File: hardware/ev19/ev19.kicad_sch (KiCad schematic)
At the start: 163 parts, among them CN1 Conn_05x02_Female, J1 USB_C_Receptacle, J10 USB_C_Receptacle, J11 Conn_02x05_Counter_Clockwise, J2 Conn_01x02_Socket, J4 Conn_02x03_Odd_Even, J5 Conn_02x03_Odd_Even, J6 Conn_02x05_Counter_Clockwise, J7 Conn_02x05_Counter_Clockwise, J8 Conn_02x05_Counter_Clockwise, J9 Conn_02x05_Counter_Clockwise, Q1 2N7002, Q2 2N7002, Q3 2N7002, Q4 2N7002, SW1 SW_SPDT, SW2 SW_Push, SW3 SW_Push, U1 BQ21040DBV, U12 XC6227C301MR-G, U2 USBLC6-2P6, U3 STM32F072CBTx, U4 CH340C, U5 TPS63060, U7 ESP32-S3-WROOM-1, U9 TPS2116DRL, Y1 Crystal_GND24

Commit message: Added missing footprints, used kicad10 wizard tool to design them, designed starting point of the board layout
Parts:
- removed J10: USB_C_Receptacle, Connector_USB:USB_C_Receptacle_HRO_TYPE-C-31-M-12, symbol Connector:USB_C_Receptacle_USB2.0_16P
- added H5: MountingHole, MountingHole:MountingHole_2.7mm_M2.5, symbol Mechanical:MountingHole
- added J13: USB_C_Receptacle_USB2.0_16P, Connector_USB:USB_C_Receptacle_HRO_TYPE-C-31-M-12, symbol Connector:USB_C_Receptacle_USB2.0_16P
- JP1: footprint (none) -> Jumper:SolderJumper-3_P1.3mm_Bridged12_RoundedPad1.0x1.5mm
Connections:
- new net: J13.A1 (GND), J13.A12 (GND), J13.B1 (GND), J13.B12 (GND)
- new net: J13.A4 (VBUS), J13.A9 (VBUS), J13.B4 (VBUS), J13.B9 (VBUS)
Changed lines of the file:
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@@
 	(rectangle
 		(start 153.67 222.25)
-		(end 180.34 247.65)
+		(end 180.34 251.46)
 		(stroke
 			(width 0)
@@
 	)
 	(symbol
+		(lib_id "Mechanical:MountingHole")
+		(at 158.75 247.65 0)
+		(unit 1)
+		(body_style 1)
+		(exclude_from_sim no)
+		(in_bom no)
+		(on_board yes)
+		(in_pos_files yes)
+		(dnp no)
+		(fields_autoplaced yes)
+		(property "Reference" "H5"
+			(at 161.29 246.3799 0)
+			(show_name no)
+			(do_not_autoplace no)
+			(effects
+				(font
+					(size 1.27 1.27)
+				)
+				(justify left)
+			)
+		)
+		(property "Value" "MountingHole"
+			(at 161.29 248.9199 0)
+			(show_name no)
+			(do_not_autoplace no)
+			(effects
+				(font
+					(size 1.27 1.27)
+				)
+				(justify left)
+			)
+		)
+		(property "Footprint" "MountingHole:MountingHole_2.7mm_M2.5"
+			(at 158.75 247.65 0)
+			(hide yes)
+			(show_name no)
+			(do_not_autoplace no)
+			(effects
+				(font
+					(size 1.27 1.27)
+				)
+			)
+		)
+		(property "Datasheet" ""
+			(at 158.75 247.65 0)
+			(hide yes)
+			(show_name no)
+			(do_not_autoplace no)
+			(effects
+				(font
+					(size 1.27 1.27)
+				)
+			)
+		)
+		(property "Description" "Mounting Hole without connection"
+			(at 158.75 247.65 0)
+			(hide yes)
+			(show_name no)
+			(do_not_autoplace no)
+			(effects
+				(font
+					(size 1.27 1.27)
+				)
+			)
+		)
+		(property "JLCPCB Position Offset" ""
+			(at 158.75 247.65 0)
+			(hide yes)
+			(show_name no)
+			(do_not_autoplace no)
+			(effects
+				(font
+					(size 1.27 1.27)
+				)
+			)
+		)
+		(property "Sim.Type" ""
+			(at 158.75 247.65 0)
+			(hide yes)
+			(show_name no)
+			(do_not_autoplace no)
+			(effects
+				(font
+					(size 1.27 1.27)
+				)
+			)
+		)
+		(instances
+			(project "ev19"
+				(path "/bd865368-262b-4f76-b7a6-1673c2cb0f8c"
+					(reference "H5")
+					(unit 1)
+				)
+			)
+		)
+	)
+	(symbol
 		(lib_id "Transistor_FET:2N7002")
 		(at 339.09 80.01 0)
@@
 	)
 	(symbol
-		(lib_id "Connector:USB_C_Receptacle_USB2.0_16P")
-		(at 539.75 345.44 0)
-		(unit 1)
-		(body_style 1)
-		(exclude_from_sim no)
-		(in_bom yes)
-		(on_board yes)
-		(in_pos_files yes)
-		(dnp no)
-		(property "Reference" "J10"
-			(at 550.164 326.644 0)
-			(show_name no)
-			(do_not_autoplace no)
-			(effects
-				(font
-					(size 1.27 1.27)
-				)
-				(justify right)
-			)
-		)
-		(property "Value" "USB_C_Receptacle"
-			(at 557.276 364.49 0)
-			(show_name no)
-			(do_not_autoplace no)
-			(effects
-				(font
-					(size 1.27 1.27)
-				)
-				(justify right)
-			)
-		)
-		(property "Footprint" "Connector_USB:USB_C_Receptacle_HRO_TYPE-C-31-M-12"
-			(at 543.56 345.44 0)
-			(hide yes)
-			(show_name no)
-			(do_not_autoplace no)
-			(effects
-				(font
-					(size 1.27 1.27)
-				)
-			)
-		)
-		(property "Datasheet" "https://www.usb.org/sites/default/files/documents/usb_type-c.zip"
-			(at 543.56 345.44 0)
-			(hide yes)
-			(show_name no)
-			(do_not_autoplace no)
-			(effects
-				(font
-					(size 1.27 1.27)
-				)
-			)
-		)
-		(property "Description" "USB 2.0-only 16P Type-C Receptacle connector"
-			(at 539.75 345.44 0)
-			(hide yes)
-			(show_name no)
-			(do_not_autoplace no)
-			(effects
-				(font
-					(size 1.27 1.27)
-				)
-			)
-		)
-		(property "JLCPCB Part #" "C165948"
-			(at 539.75 345.44 0)
-			(hide yes)
-			(show_name no)
-			(do_not_autoplace no)
-			(effects
-				(font
-					(size 1.27 1.27)
-				)
-			)
-		)
-		(property "JLCPCB Position Offset" ""
-			(at 539.75 345.44 0)
-			(hide yes)
-			(show_name no)
-			(do_not_autoplace no)
-			(effects
-				(font
-					(size 1.27 1.27)
-				)
-			)
-		)
-		(property "Sim.Type" ""
-			(at 539.75 345.44 0)
-			(hide yes)
-			(show_name no)
-			(do_not_autoplace no)
-			(effects
-				(font
-					(size 1.27 1.27)
-				)
-			)
-		)
-		(pin "A1"
-		)
-		(pin "A12"
-		)
-		(pin "A4"
-		)
-		(pin "A5"
-		)
-		(pin "A6"
-		)
-		(pin "A7"
-		)
-		(pin "A8"
-		)
-		(pin "A9"
-		)
-		(pin "B1"
-		)
-		(pin "B12"
-		)
-		(pin "B4"
-		)
-		(pin "B5"
-		)
-		(pin "B6"
-		)
-		(pin "B7"
-		)
-		(pin "B8"
-		)
-		(pin "B9"
-		)
-		(pin "S1"
-		)
-		(instances
-			(project "ev19"
-				(path "/bd865368-262b-4f76-b7a6-1673c2cb0f8c"
-					(reference "J10")
-					(unit 1)
-				)
-			)
-		)
-	)
-	(symbol
 		(lib_id "Device:R_US")
 		(at 29.21 350.52 0)
@@
 	)
 	(symbol
+		(lib_name "USB_C_Receptacle_USB2.0_16P_1")
+		(lib_id "Connector:USB_C_Receptacle_USB2.0_16P")
+		(at 539.75 345.44 0)
+		(unit 1)
+		(body_style 1)
+		(exclude_from_sim no)
+		(in_bom yes)
+		(on_board yes)
+		(in_pos_files yes)
+		(dnp no)
+		(fields_autoplaced yes)
+		(property "Reference" "J13"
+			(at 539.75 322.58 0)
+			(show_name no)
+			(do_not_autoplace no)
+			(effects
+				(font
+					(size 1.27 1.27)
+				)
+			)
+		)
+		(property "Value" "USB_C_Receptacle_USB2.0_16P"
+			(at 539.75 325.12 0)
+			(show_name no)
+			(do_not_autoplace no)
+			(effects
+				(font
+					(size 1.27 1.27)
+				)
+			)
+		)
+		(property "Footprint" "Connector_USB:USB_C_Receptacle_HRO_TYPE-C-31-M-12"
+			(at 543.56 345.44 0)
+			(hide yes)
+			(show_name no)
+			(do_not_autoplace no)
+			(effects
+				(font
+					(size 1.27 1.27)
+				)
+			)
+		)
+		(property "Datasheet" "https://www.usb.org/sites/default/files/documents/usb_type-c.zip"
+			(at 543.56 345.44 0)
+			(hide yes)
+			(show_name no)
+			(do_not_autoplace no)
+			(effects
+				(font
+					(size 1.27 1.27)
+				)
+			)
+		)
+		(property "Description" "USB 2.0-only 16P Type-C Receptacle connector"
+			(at 539.75 345.44 0)
+			(hide yes)
+			(show_name no)
+			(do_not_autoplace no)
+			(effects
+				(font
+					(size 1.27 1.27)
+				)
+			)
+		)
+		(pin "A6"
+		)
+		(pin "B12"
+		)
+		(pin "B6"
+		)
+		(pin "A8"
+		)
+		(pin "B5"
+		)
+		(pin "B9"
+		)
+		(pin "B8"
+		)
+		(pin "B7"
+		)
+		(pin "A9"
+		)
+		(pin "A12"
+		)
+		(pin "SH"
+		)
+		(pin "A1"
+		)
+		(pin "A7"
+		)
+		(pin "B1"
+		)
+		(pin "B4"
+		)
+		(pin "A5"
+		)
+		(pin "A4"
+		)
+		(instances
+			(project "ev19"
+				(path "/bd865368-262b-4f76-b7a6-1673c2cb0f8c"
+					(reference "J13")
+					(unit 1)
+				)
+			)
+		)
+	)
+	(symbol
 		(lib_id "Connector:TestPoint")
 		(at 410.21 312.42 270)
@@
 			)
 		)
-		(property "Footprint" ""
+		(property "Footprint" "Jumper:SolderJumper-3_P1.3mm_Bridged12_RoundedPad1.0x1.5mm"
 			(at 34.29 346.71 0)
 			(hide yes)

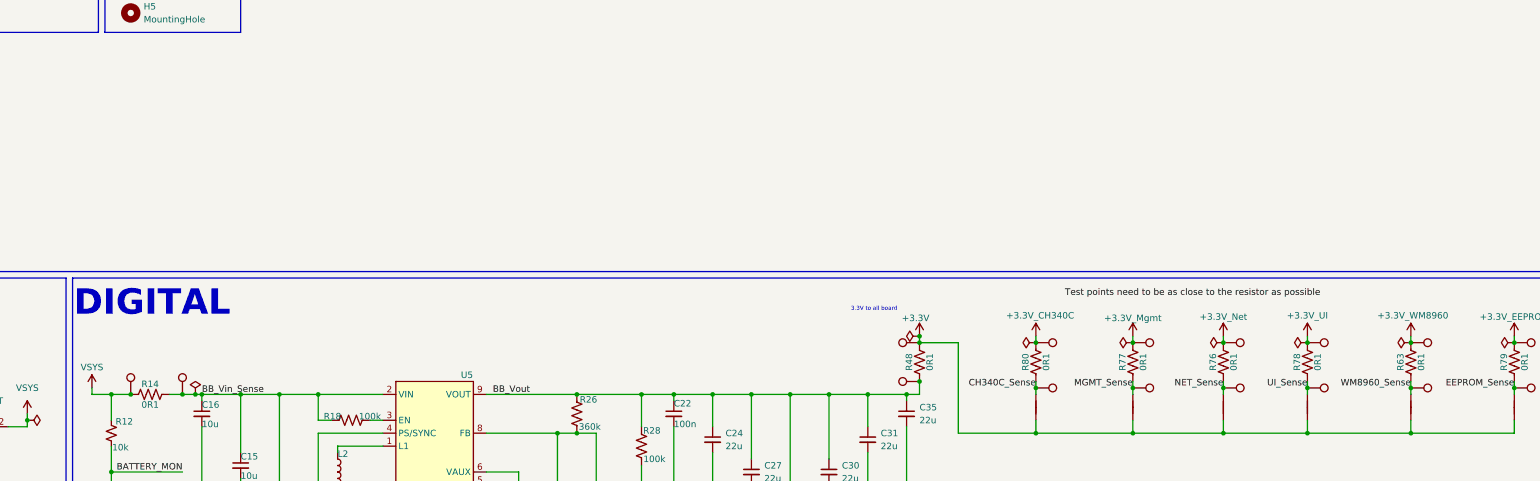
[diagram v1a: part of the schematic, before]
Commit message: Fixed a couple mistakes on the schematic, got general power layout of the hactar designed, finding layout for audio section
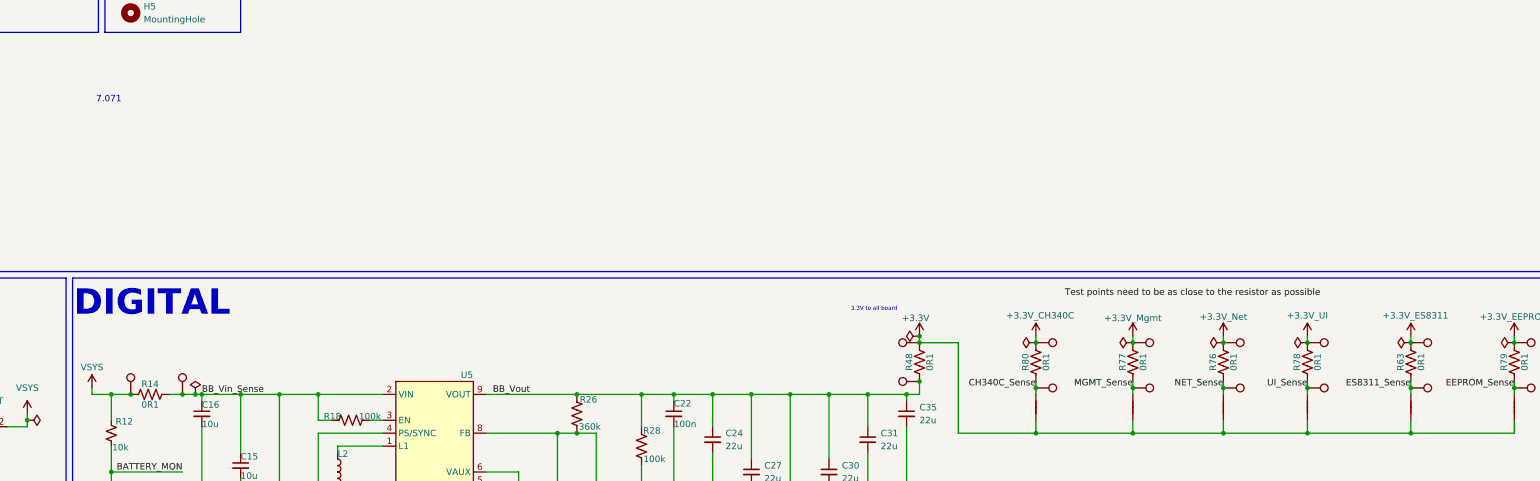
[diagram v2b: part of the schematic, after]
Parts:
- U7: footprint RF_Module:ESP32-S3-WROOM-1 -> Hactar_Footprints:ESP32-S3-WROOM-1
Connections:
- net +3.3V_WM8960 renamed +3.3V_ES8311
- net WM8960_Sense renamed ES8311_Sense
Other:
- note added: "7.071"
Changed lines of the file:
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@@
 		)
 	)
+	(text "7.071\n"
+		(exclude_from_sim no)
+		(at 154.432 264.668 0)
+		(effects
+			(font
+				(size 1.27 1.27)
+			)
+		)
+	)
 	(text "USB"
 		(exclude_from_sim no)
@@
 		)
 	)
-	(label "WM8960_Sense"
+	(label "ES8311_Sense"
 		(at 410.21 321.31 180)
 		(effects
@@
 			)
 		)
-		(property "Footprint" "RF_Module:ESP32-S3-WROOM-1"
+		(property "Footprint" "Hactar_Footprints:ESP32-S3-WROOM-1"
 			(at 262.89 81.28 0)
 			(hide yes)
@@
 			)
 		)
-		(property "Value" "+3.3V_WM8960"
+		(property "Value" "+3.3V_ES8311"
 			(at 417.576 307.086 0)
 			(show_name no)
